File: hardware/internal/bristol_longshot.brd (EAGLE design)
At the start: 14 x 62 mm, 39 parts, among them U1 SAM_D20E, U15 BMP180, U2 SI4060, U7 TPS3123, U8 SN74LVC1G32DCKR

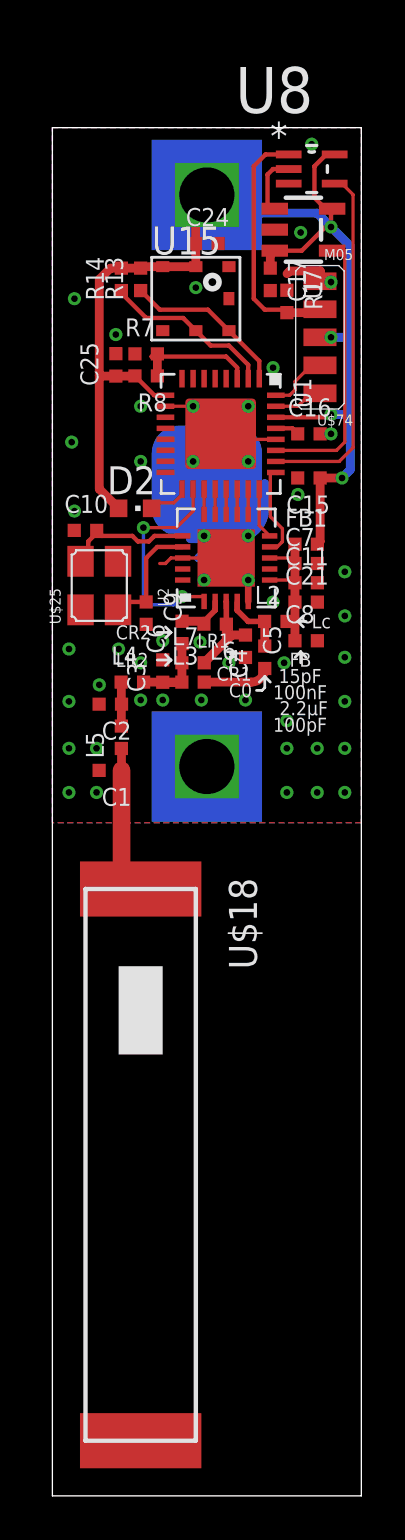
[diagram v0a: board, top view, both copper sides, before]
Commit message: Updated main solar active components names to correspond with partslist
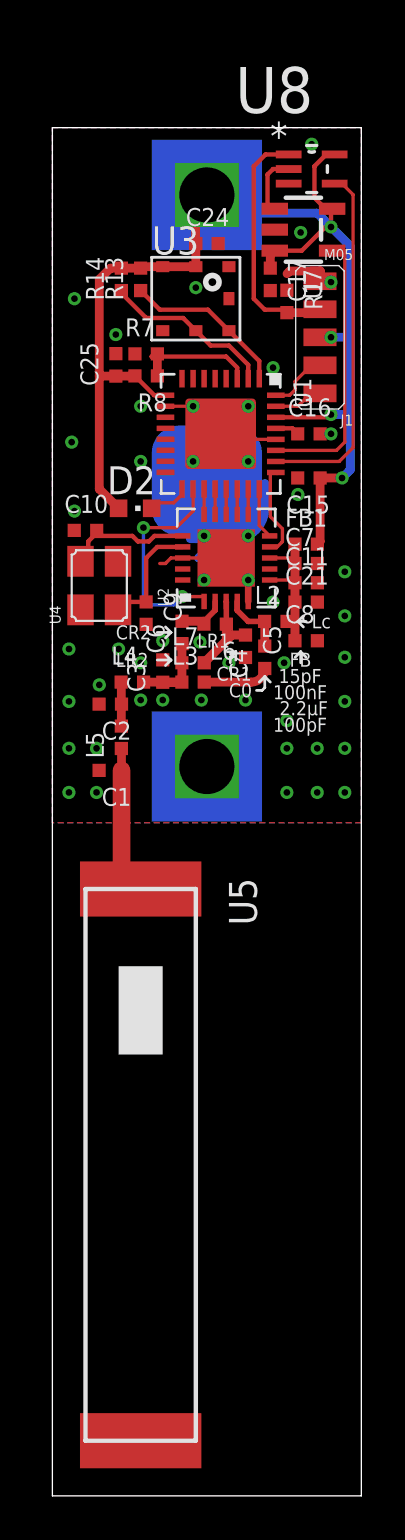
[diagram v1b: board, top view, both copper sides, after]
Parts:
- renumbered U$18 to U5, U$19 to J2, U$25 to U4, U$74 to J1, U15 to U3

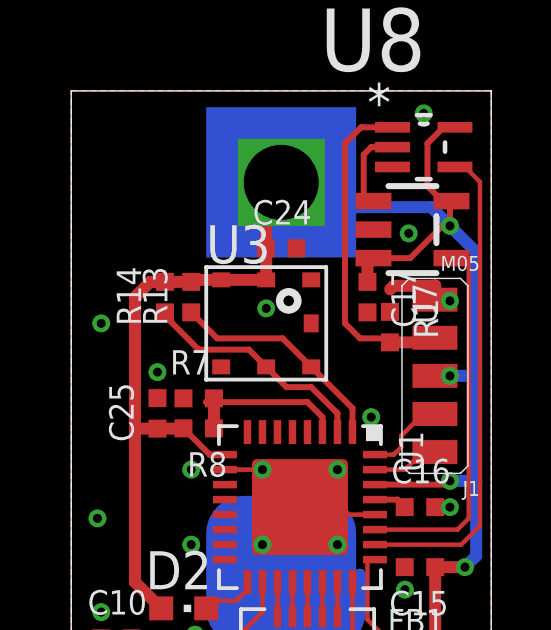
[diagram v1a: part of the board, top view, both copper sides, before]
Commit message: Updated many parts lists, updated bard numbering, removed makefiles for inactive things
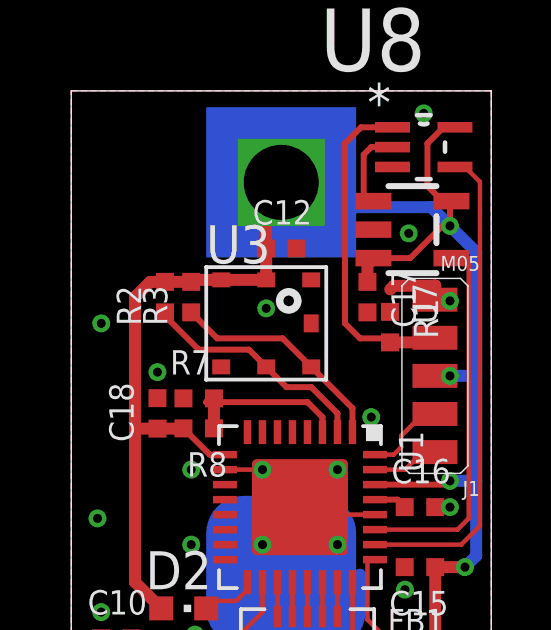
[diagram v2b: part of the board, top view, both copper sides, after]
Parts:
- R2, R3: value 1kΩ -> 10kΩ
- renumbered C24 to C12, C25 to C18, R13 to R3, R14 to R2
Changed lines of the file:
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@@
 <element name="R8" library="microbuilder_v3" package="_0402" value="22kΩ" x="4.25" y="50.75" rot="R180"/>
 <element name="U3" library="SparkFun-Sensors" package="BMP180" value="BMP180" x="6.5" y="54.25"/>
-<element name="C24" library="microbuilder_v3" package="_0402" value="100nF" x="7" y="56.75"/>
-<element name="C25" library="microbuilder_v3" package="_0402" value="4.7µF" x="2.875" y="51.25" rot="R90"/>
-<element name="R13" library="microbuilder_v3" package="_0402" value="1kΩ" x="4" y="55.125" rot="R90"/>
-<element name="R14" library="microbuilder_v3" package="_0402" value="1kΩ" x="3.125" y="55.125" rot="R90"/>
+<element name="C12" library="microbuilder_v3" package="_0402" value="100nF" x="7" y="56.75"/>
+<element name="C18" library="microbuilder_v3" package="_0402" value="4.7µF" x="2.875" y="51.25" rot="R90"/>
+<element name="R3" library="microbuilder_v3" package="_0402" value="10kΩ" x="4" y="55.125" rot="R90"/>
+<element name="R2" library="microbuilder_v3" package="_0402" value="10kΩ" x="3.125" y="55.125" rot="R90"/>
 <element name="U5" library="fbri" package="0433AT62A0020E" value="0433AT62A0020E" x="4" y="15" rot="R180"/>
 <element name="J2" library="fbri" package="BC-2001" value="BC-2001" x="7" y="46" rot="MR270"/>
@@
 <via x="6.5" y="54.75" extent="1-16" drill="0.3"/>
 <contactref element="U3" pad="7"/>
-<contactref element="C24" pad="2"/>
-<contactref element="C25" pad="2"/>
+<contactref element="C12" pad="2"/>
+<contactref element="C18" pad="2"/>
 <contactref element="J2" pad="-VE"/>
 <via x="2.125" y="36.75" extent="1-16" drill="0.3"/>
@@
 <contactref element="C10" pad="1"/>
 <contactref element="C9" pad="2"/>
-<wire x1="10.7086" y1="59.4646" x2="11.75" y2="61.25" width="0" layer="19" extent="1-1"/>
-<wire x1="10.0749" y1="57.375" x2="10.7086" y2="59.4646" width="0" layer="19" extent="1-1"/>
-<wire x1="11.25" y1="57.25" x2="10.0749" y2="57.375" width="0" layer="19" extent="1-1"/>
-<wire x1="10.75" y1="55.5" x2="11.25" y2="57.25" width="0" layer="19" extent="1-1"/>
-<wire x1="12.625" y1="55" x2="12.125" y2="55.04" width="0" layer="19" extent="1-1"/>
-<wire x1="10.625" y1="54.633" x2="10.633" y2="55.383" width="0" layer="19" extent="1-1"/>
-<wire x1="9.875" y1="54.617" x2="10.625" y2="54.633" width="0" layer="19" extent="1-1"/>
-<wire x1="8" y1="54.25" x2="9.875" y2="54.617" width="0" layer="19" extent="1-1"/>
-<wire x1="6.5" y1="54.75" x2="8" y2="54.25" width="0" layer="19" extent="1-1"/>
-<wire x1="7.508" y1="56.75" x2="6.5" y2="54.75" width="0" layer="19" extent="1-1"/>
-<wire x1="10" y1="51.125" x2="9.875" y2="54.617" width="0" layer="19" extent="1-1"/>
-<wire x1="8.875" y1="49.375" x2="10" y2="51.125" width="0" layer="19" extent="1-1"/>
-<wire x1="4" y1="49.375" x2="5.125" y2="49.375" width="0" layer="19" extent="1-1"/>
-<wire x1="9.625" y1="45.875" x2="8.875" y2="46.875" width="0" layer="19" extent="16-16"/>
-<wire x1="6.625" y1="42.5" x2="6.625" y2="42.5" width="0" layer="19" extent="1-16"/>
-<wire x1="8.875" y1="43.5" x2="8.25" y2="43.375" width="0" layer="19" extent="16-16"/>
-<wire x1="8.875" y1="41.5" x2="7.875" y2="42.5" width="0" layer="19" extent="1-1"/>
-<wire x1="10" y1="40.5" x2="8.875" y2="40.53" width="0" layer="19" extent="1-1"/>
-<wire x1="11.117" y1="46.125" x2="9.625" y2="45.875" width="0" layer="19" extent="1-16"/>
-<wire x1="11.125" y1="45.375" x2="11.117" y2="46.125" width="0" layer="19" extent="1-1"/>
-<wire x1="6.375" y1="46.875" x2="7.625" y2="48.125" width="0" layer="19" extent="1-1"/>
-<wire x1="12.008" y1="40.5" x2="10" y2="40.5" width="0" layer="19" extent="1-1"/>
-<wire x1="12.008" y1="41.375" x2="12.008" y2="40.5" width="0" layer="19" extent="1-1"/>
-<wire x1="12.008" y1="42.25" x2="12.008" y2="41.375" width="0" layer="19" extent="1-1"/>
-<wire x1="13.25" y1="41.875" x2="12.008" y2="42.25" width="0" layer="19" extent="1-1"/>
-<wire x1="13.25" y1="39.875" x2="12.008" y2="40.5" width="0" layer="19" extent="1-1"/>
-<wire x1="12.008" y1="38.75" x2="13.25" y2="39.875" width="0" layer="19" extent="1-1"/>
-<wire x1="13.25" y1="38" x2="12.008" y2="38.75" width="0" layer="19" extent="1-1"/>
-<wire x1="10.5" y1="37.75" x2="12.008" y2="38.75" width="0" layer="19" extent="1-1"/>
-<wire x1="8.75" y1="37.992" x2="10.5" y2="37.75" width="0" layer="19" extent="1-1"/>
-<wire x1="8" y1="37.75" x2="8.75" y2="37.992" width="0" layer="19" extent="1-1"/>
-<wire x1="6.6875" y1="38.6875" x2="8" y2="37.75" width="0" layer="19" extent="1-1"/>
-<wire x1="5" y1="38.75" x2="6.6875" y2="38.6875" width="0" layer="19" extent="1-1"/>
-<wire x1="5" y1="37.883" x2="5" y2="38.75" width="0" layer="19" extent="1-1"/>
-<wire x1="4" y1="37.75" x2="5" y2="37.883" width="0" layer="19" extent="1-1"/>
-<wire x1="4.25" y1="39.492" x2="5" y2="38.75" width="0" layer="19" extent="1-1"/>
-<wire x1="3" y1="38.375" x2="4" y2="37.75" width="0" layer="19" extent="1-1"/>
-<wire x1="4" y1="36.0625" x2="4" y2="37.75" width="0" layer="19" extent="1-1"/>
-<wire x1="5" y1="36.0625" x2="4" y2="36.0625" width="0" layer="19" extent="1-1"/>
-<wire x1="6.75" y1="36.0625" x2="5" y2="36.0625" width="0" layer="19" extent="1-1"/>
-<wire x1="8.75" y1="36.0625" x2="8" y2="37.75" width="0" layer="19" extent="1-1"/>
-<wire x1="2.125" y1="36.75" x2="3" y2="38.375" width="0" layer="19" extent="1-1"/>
-<wire x1="2.117" y1="35.875" x2="2.125" y2="36.75" width="0" layer="19" extent="1-1"/>
-<wire x1="0.75" y1="36" x2="2.117" y2="35.875" width="0" layer="19" extent="1-1"/>
-<wire x1="13.25" y1="36" x2="13.25" y2="38" width="0" layer="19" extent="1-1"/>
-<wire x1="2" y1="33.875" x2="2.117" y2="35.875" width="0" layer="19" extent="1-1"/>
-<wire x1="2.117" y1="32.875" x2="2" y2="33.875" width="0" layer="19" extent="1-1"/>
-<wire x1="2" y1="31.875" x2="2.117" y2="32.875" width="0" layer="19" extent="1-1"/>
-<wire x1="0.75" y1="33.875" x2="2" y2="33.875" width="0" layer="19" extent="1-1"/>
-<wire x1="0.75" y1="31.875" x2="2" y2="31.875" width="0" layer="19" extent="1-1"/>
-<wire x1="12.133" y1="48.125" x2="10.125" y2="47.875" width="0" layer="19" extent="1-1"/>
-<wire x1="12.625" y1="48.125" x2="12.133" y2="48.125" width="0" layer="19" extent="1-1"/>
-<wire x1="10.625" y1="35.125" x2="8.75" y2="36.0625" width="0" layer="19" extent="1-1"/>
-<wire x1="10.625" y1="33.875" x2="10.625" y2="35.125" width="0" layer="19" extent="1-1"/>
-<wire x1="12" y1="33.875" x2="10.625" y2="33.875" width="0" layer="19" extent="1-1"/>
-<wire x1="13.25" y1="33.875" x2="12" y2="33.875" width="0" layer="19" extent="1-1"/>
-<wire x1="13.25" y1="31.875" x2="13.25" y2="33.875" width="0" layer="19" extent="1-1"/>
-<wire x1="12" y1="31.875" x2="13.25" y2="31.875" width="0" layer="19" extent="1-1"/>
-<wire x1="10.625" y1="31.875" x2="12" y2="31.875" width="0" layer="19" extent="1-1"/>
-<wire x1="0.75" y1="38.375" x2="2.125" y2="36.75" width="0" layer="19" extent="1-1"/>
-<wire x1="4" y1="46.875" x2="6.375" y2="46.875" width="0" layer="19" extent="1-1"/>
-<wire x1="3.742" y1="51.75" x2="4" y2="49.375" width="0" layer="19" extent="1-1"/>
-<wire x1="2.875" y1="51.758" x2="3.742" y2="51.75" width="0" layer="19" extent="1-1"/>
-<wire x1="2.875" y1="52.625" x2="2.875" y2="51.758" width="0" layer="19" extent="1-1"/>
-<wire x1="1" y1="54.25" x2="2.875" y2="52.625" width="0" layer="19" extent="1-1"/>
-<wire x1="0.875" y1="47.75" x2="4" y2="46.875" width="0" layer="19" extent="1-1"/>
-<wire x1="1" y1="44.625" x2="0.875" y2="47.75" width="0" layer="19" extent="1-1"/>
-<wire x1="0.992" y1="43.75" x2="1" y2="44.625" width="0" layer="19" extent="1-1"/>
 </signal>
 <signal name="SWDIO">
@@
 <wire x1="10.0749" y1="56.425" x2="9.875" y2="56.2251" width="0.4" layer="1"/>
 <wire x1="9.875" y1="56.2251" x2="9.875" y2="55.633" width="0.4" layer="1"/>
-<contactref element="R14" pad="2"/>
-<contactref element="R13" pad="2"/>
-<contactref element="C24" pad="1"/>
+<contactref element="R2" pad="2"/>
+<contactref element="R3" pad="2"/>
+<contactref element="C12" pad="1"/>
 <contactref element="U3" pad="2"/>
 <contactref element="U3" pad="3"/>
-<contactref element="C25" pad="1"/>
+<contactref element="C18" pad="1"/>
 <wire x1="5" y1="55.7" x2="4.067" y2="55.7" width="0.4" layer="1"/>
 <wire x1="4.067" y1="55.7" x2="4" y2="55.633" width="0.4" layer="1"/>
@@
 <contactref element="U1" pad="1"/>
 <contactref element="U3" pad="6"/>
-<contactref element="R13" pad="1"/>
+<contactref element="R3" pad="1"/>
 <wire x1="8.125" y1="52.75" x2="8.175" y2="52.8" width="0.2" layer="1"/>
 <wire x1="8.175" y1="52.8" x2="8" y2="52.8" width="0.2" layer="1"/>
@@
 <contactref element="U1" pad="2"/>
 <contactref element="U3" pad="5"/>
-<contactref element="R14" pad="1"/>
+<contactref element="R2" pad="1"/>
 <wire x1="8.875" y1="50.625" x2="8.875" y2="51.25" width="0.2" layer="1"/>
 <wire x1="8.875" y1="51.25" x2="8" y2="52.125" width="0.2" layer="1"/>
